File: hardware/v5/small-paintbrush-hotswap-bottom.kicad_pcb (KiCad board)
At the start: 2 copper layers, 97 x 50 mm, 4 parts

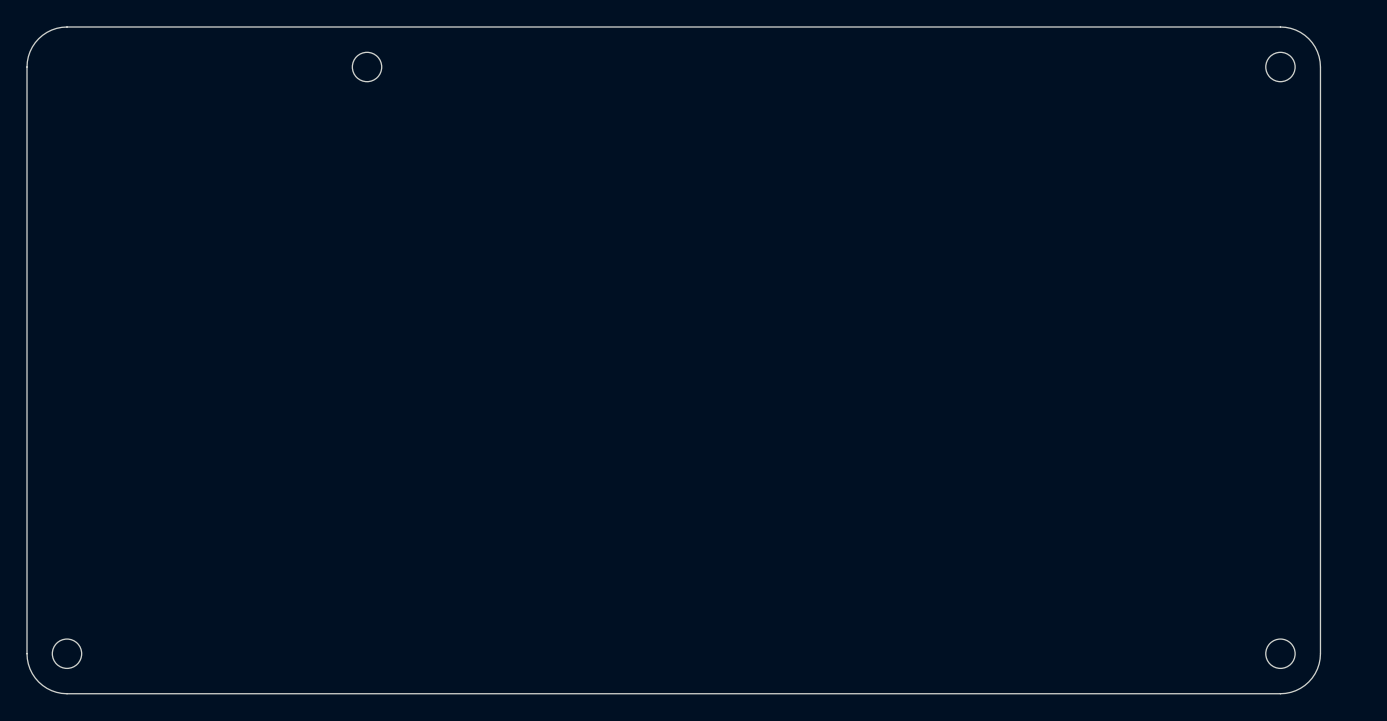
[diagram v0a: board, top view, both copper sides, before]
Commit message: v5 of the paintbrush with choc and mx hot swap switches (pcb size changed)
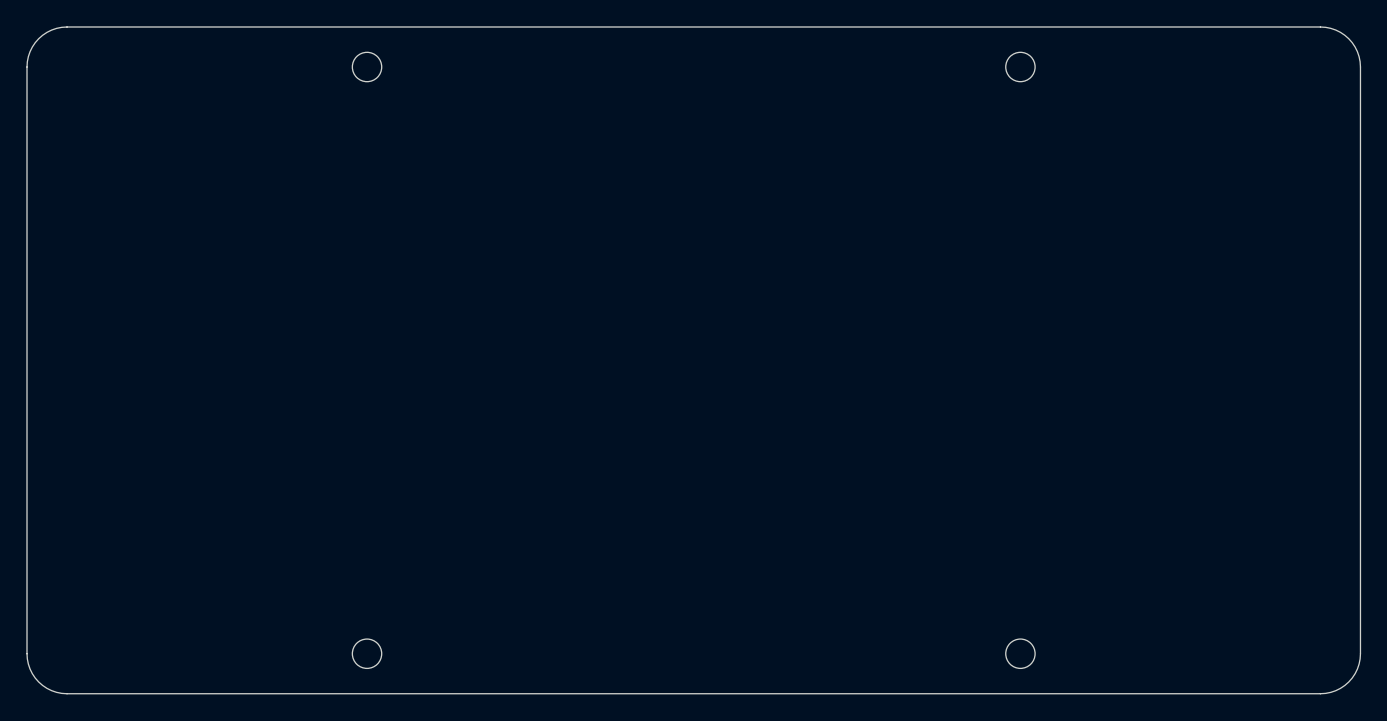
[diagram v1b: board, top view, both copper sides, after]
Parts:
- removed the REF** at (166.9, 21.6)
- removed the REF** at (166.9, 65.6)
- removed the REF** at (75.9, 65.6)
- added REF**: MountingHole_2.2mm_M2, MountingHole:MountingHole_2.2mm_M2, F.Cu at (147.4, 65.6)
- added REF**: MountingHole_2.2mm_M2, MountingHole:MountingHole_2.2mm_M2, F.Cu at (147.4, 21.6)
- added REF**: MountingHole_2.2mm_M2, MountingHole:MountingHole_2.2mm_M2, F.Cu at (98.4, 65.6)
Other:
- board size 97 x 50 mm -> 100 x 50 mm
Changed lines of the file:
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@@
   (general
     (thickness 1.6)
-    (drawings 8)
+    (drawings 12)
     (tracks 0)
     (zones 0)
@@
     (47 F.CrtYd user hide)
     (48 B.Fab user)
-    (49 F.Fab user)
+    (49 F.Fab user hide)
   )
   (setup
@@
     (visible_elements FFFFFF7F)
     (pcbplotparams
-      (layerselection 0x010f0_ffffffff)
+      (layerselection 0x01000_7ffffffe)
       (usegerberextensions false)
       (usegerberattributes true)
@@
       (padsonsilk false)
       (subtractmaskfromsilk false)
-      (outputformat 1)
+      (outputformat 5)
       (mirror false)
       (drillshape 0)
@@
   )
   (module MountingHole:MountingHole_2.2mm_M2 (layer F.Cu)
-    (at 166.901737 21.599424)
+    (at 147.401736 65.599424)
     (descr "Mounting Hole 2.2mm, no annular, M2")
     (tags "mounting hole 2.2mm no annular m2")
+    (attr virtual)
     (fp_text reference REF** (at 0 -3.2) (layer F.SilkS) hide
       (effects (font (size 1 1) (thickness 0.15)))
@@
     (fp_circle (center 0 0) (end 2.45 0) (layer F.CrtYd) (width 0.05))
     (fp_circle (center 0 0) (end 2.2 0) (layer Cmts.User) (width 0.15))
+    (fp_text user %R (at 0.3 0) (layer F.Fab)
+      (effects (font (size 1 1) (thickness 0.15)))
+    )
     (pad 1 np_thru_hole circle (at 0 0) (size 2.2 2.2) (drill 2.2) (layers *.Cu *.Mask))
   )
   (module MountingHole:MountingHole_2.2mm_M2 (layer F.Cu)
-    (at 166.901739 65.599426)
+    (at 147.401736 21.599424)
     (descr "Mounting Hole 2.2mm, no annular, M2")
     (tags "mounting hole 2.2mm no annular m2")
+    (attr virtual)
+    (fp_text reference REF** (at 0 -3.2) (layer F.SilkS) hide
+      (effects (font (size 1 1) (thickness 0.15)))
+    )
+    (fp_text value MountingHole_2.2mm_M2 (at -78.199994 40.5 270) (layer F.Fab)
+      (effects (font (size 1 1) (thickness 0.15)))
+    )
+    (fp_circle (center 0 0) (end 2.45 0) (layer F.CrtYd) (width 0.05))
+    (fp_circle (center 0 0) (end 2.2 0) (layer Cmts.User) (width 0.15))
+    (fp_text user %R (at 0.3 0) (layer F.Fab)
+      (effects (font (size 1 1) (thickness 0.15)))
+    )
+    (pad 1 np_thru_hole circle (at 0 0) (size 2.2 2.2) (drill 2.2) (layers *.Cu *.Mask))
+  )
+  (module MountingHole:MountingHole_2.2mm_M2 (layer F.Cu)
+    (at 98.401735 65.599424)
+    (descr "Mounting Hole 2.2mm, no annular, M2")
+    (tags "mounting hole 2.2mm no annular m2")
+    (attr virtual)
     (fp_text reference REF** (at 0 -3.2) (layer F.SilkS) hide
       (effects (font (size 1 1) (thickness 0.15)))
@@
     (fp_circle (center 0 0) (end 2.45 0) (layer F.CrtYd) (width 0.05))
     (fp_circle (center 0 0) (end 2.2 0) (layer Cmts.User) (width 0.15))
+    (fp_text user %R (at 0.3 0) (layer F.Fab)
+      (effects (font (size 1 1) (thickness 0.15)))
+    )
     (pad 1 np_thru_hole circle (at 0 0) (size 2.2 2.2) (drill 2.2) (layers *.Cu *.Mask))
   )
@@
     (pad 1 np_thru_hole circle (at 0 0) (size 2.2 2.2) (drill 2.2) (layers *.Cu *.Mask))
   )
-  (module MountingHole:MountingHole_2.2mm_M2 (layer F.Cu)
-    (at 75.901739 65.599424)
-    (descr "Mounting Hole 2.2mm, no annular, M2")
-    (tags "mounting hole 2.2mm no annular m2")
-    (fp_text reference REF** (at 0 -3.2) (layer F.SilkS) hide
-      (effects (font (size 1 1) (thickness 0.15)))
-    )
-    (fp_text value MountingHole_2.2mm_M2 (at 0 3.2) (layer F.Fab)
-      (effects (font (size 1 1) (thickness 0.15)))
-    )
-    (fp_circle (center 0 0) (end 2.45 0) (layer F.CrtYd) (width 0.05))
-    (fp_circle (center 0 0) (end 2.2 0) (layer Cmts.User) (width 0.15))
-    (pad 1 np_thru_hole circle (at 0 0) (size 2.2 2.2) (drill 2.2) (layers *.Cu *.Mask))
-  )
+  (gr_circle (center 98.401736 21.599424) (end 99.501736 21.599424) (layer Eco1.User) (width 0.15))
+  (gr_circle (center 147.401736 21.599424) (end 148.501736 21.599424) (layer Eco1.User) (width 0.15))
+  (gr_circle (center 147.401736 65.599424) (end 148.501736 65.599424) (layer Eco1.User) (width 0.15))
+  (gr_circle (center 98.401736 65.599424) (end 99.501736 65.599424) (layer Eco1.User) (width 0.15))
   (gr_line (start 72.901739 65.599426) (end 72.901736 21.599422) (layer Edge.Cuts) (width 0.05))
   (gr_arc (start 75.901739 65.599424) (end 72.901739 65.599426) (angle -90) (layer Edge.Cuts) (width 0.05))
-  (gr_arc (start 166.901739 65.599426) (end 166.901737 68.599424) (angle -90) (layer Edge.Cuts) (width 0.05))
+  (gr_arc (start 169.901739 65.599426) (end 169.901737 68.599424) (angle -90) (layer Edge.Cuts) (width 0.05))
   (gr_arc (start 75.901736 21.599424) (end 75.901738 18.599424) (angle -90) (layer Edge.Cuts) (width 0.05))
-  (gr_line (start 169.901739 21.599423) (end 169.901737 65.599428) (layer Edge.Cuts) (width 0.05))
-  (gr_arc (start 166.901737 21.599424) (end 169.901739 21.599423) (angle -90) (layer Edge.Cuts) (width 0.05))
-  (gr_line (start 75.901738 18.599424) (end 166.901737 18.599423) (layer Edge.Cuts) (width 0.05))
-  (gr_line (start 166.901737 68.599424) (end 75.901741 68.599424) (layer Edge.Cuts) (width 0.05))
+  (gr_line (start 172.901739 21.599423) (end 172.901737 65.599428) (layer Edge.Cuts) (width 0.05))
+  (gr_arc (start 169.901737 21.599424) (end 172.901739 21.599423) (angle -90) (layer Edge.Cuts) (width 0.05))
+  (gr_line (start 75.901738 18.599424) (end 169.901736 18.599422) (layer Edge.Cuts) (width 0.05))
+  (gr_line (start 169.901737 68.599424) (end 75.901741 68.599424) (layer Edge.Cuts) (width 0.05))
 )
